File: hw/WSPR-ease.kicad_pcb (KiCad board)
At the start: 4 copper layers, 99 x 64 mm, 134 parts, among them J101 SMA, J102 SMA, J103 pwr+data, Q101 MMBF170, Q301 MMBF170, Q302 MMBF170, Q303 MMBF170, Q304 MMBF170, Q305 MMBF170, Q306 MMBF170, Q307 MMBF170, Q308 MMBF170, Q309 MMBF170, Q310 MMBF170, Q311 MMBF170, Q312 MMBF170, T301 BN-43-202_DualPri_CTSec, U101 GNSS module, U102 ESP32-S3-WROOM-1-N8R8, U103 SRV05-4, U104 TPS22918DBVR, U105 TPS74612PQWDRBRQ1, U106 LMR51430YDDCR, U201 AS183-92LF, U202 AS183-92LF, U203 AS183-92LF, U204 AS183-92LF, U301 ICE40UP5K-SG48ITR, U302 CD74ACT541SM96, Y301 40MHz

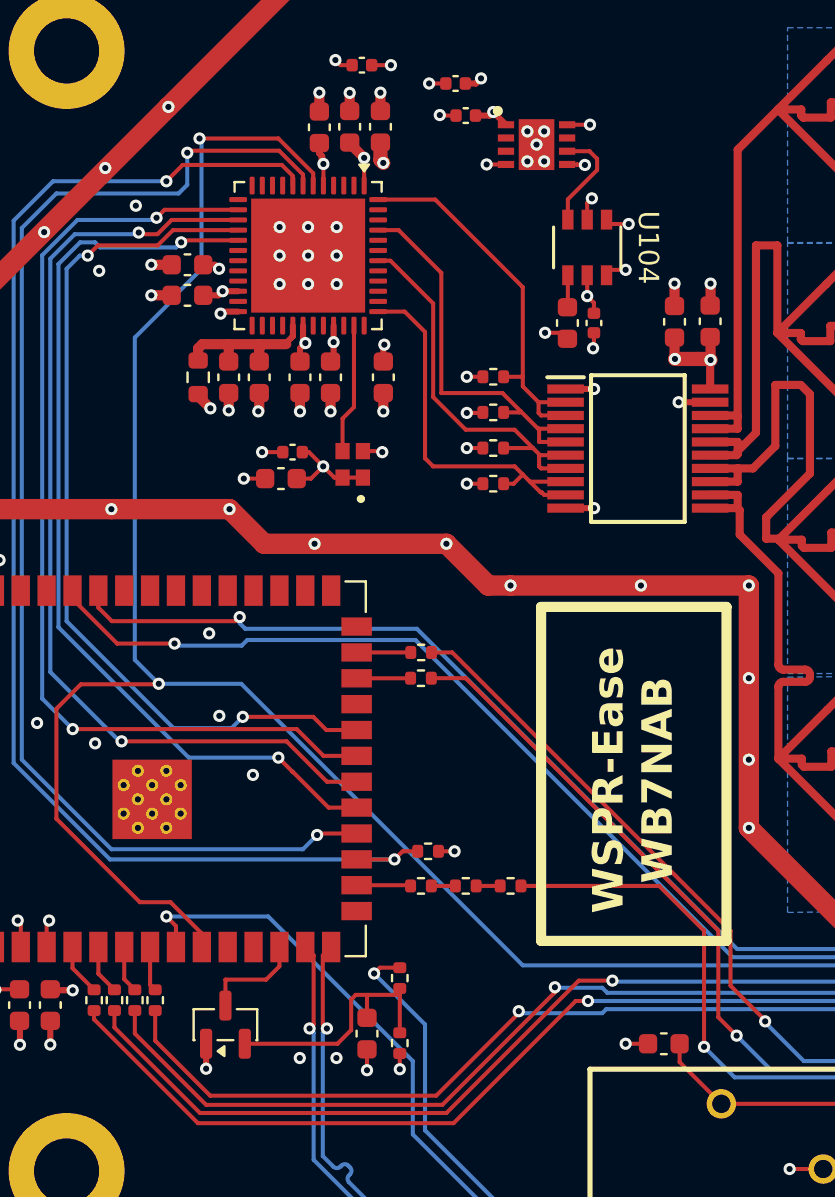
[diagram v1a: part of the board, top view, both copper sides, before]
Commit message: Still working on FPGA config loading. Problem is now CMOS lockup caused by FPGACORE vs FPGAIO rails. I moved FPGAIO enable to IO42 on ESP32 and pgFPGACORE to IO41.
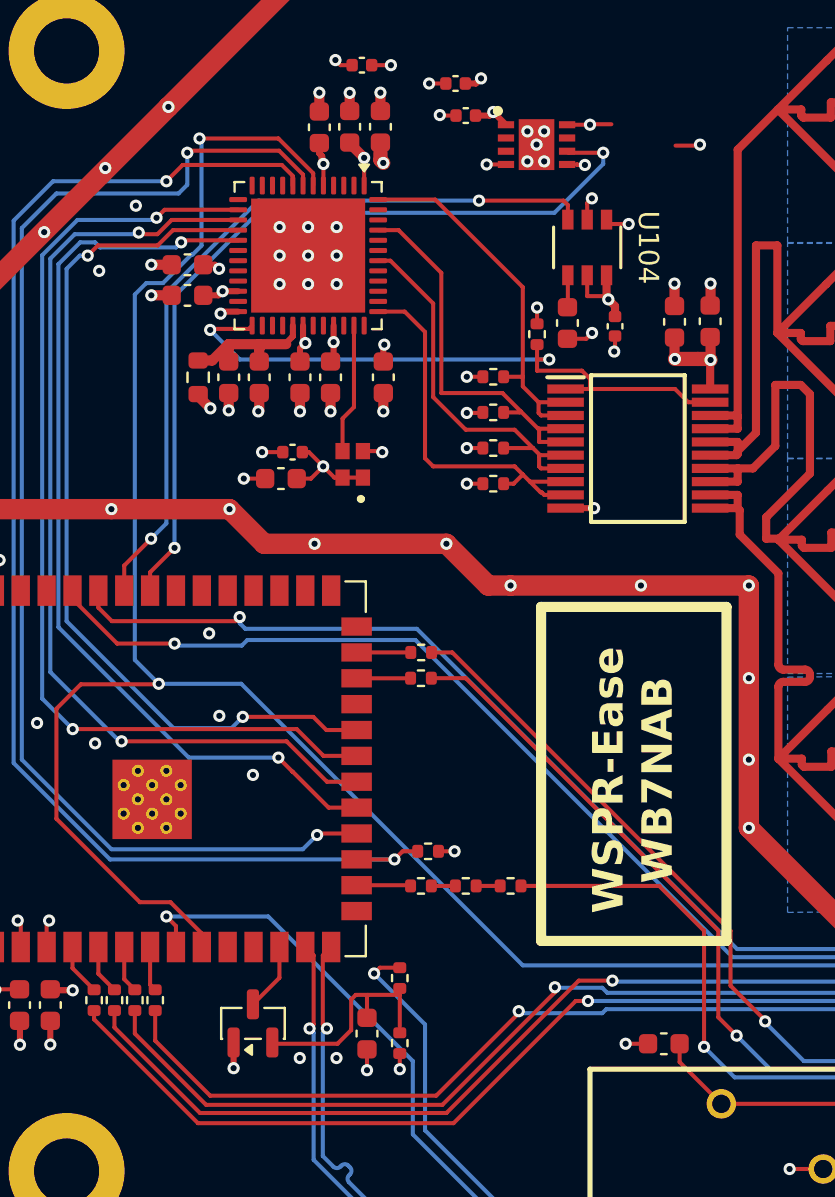
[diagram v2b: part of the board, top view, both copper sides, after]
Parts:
- added R319: 10k, Resistor_SMD:R_0402_1005Metric, F.Cu at (77.7, 87.3)
- moved Q101 1.35 mm to (63.8, 121.2)
- moved C109 1.05 mm to (81.5, 86.9)
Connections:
- U102 pad 34: unconnected-(U102-IO41-Pad34) -> /pgFPGACORE
- U102 pad 35: unconnected-(U102-IO42-Pad35) -> /enFPGAIO
- U104 pad 3: Net-(U104-ON) -> /enFPGAIO
- U105 pad 6: Net-(U104-ON) -> /pgFPGACORE
- U301 pad 25: unconnected-(U301A-IOT_36b-Pad25) -> /Transmitter/driverNEN
- U302 pad 1: GND -> /Transmitter/driverNEN
- U302 pad 19: GND -> /Transmitter/driverNEN
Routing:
- net /pgFPGACORE: track 0.00 -> 41.1 mm, vias 0 -> 2
- net /enFPGAIO: track 0.00 -> 37.9 mm, vias 0 -> 2
- net /Transmitter/driverNEN: track 0.00 -> 31.9 mm, vias 0 -> 2
- net Net-(U104-ON): track 5.44 -> 0.00 mm
- net +3.3V: track 23.1 -> 25.0 mm, vias 16 -> 17
- net Net-(Q101-D): track 5.14 -> 3.35 mm
- net GND: track 336.9 -> 335.4 mm, vias 162 -> 161
- net +VFPGAIO: track 22.5 -> 23.9 mm, vias 12 -> 11
- net Net-(Q101-S): track 12.2 -> 10.8 mm
- net /gnssPPS: track 131.2 -> 131.7 mm

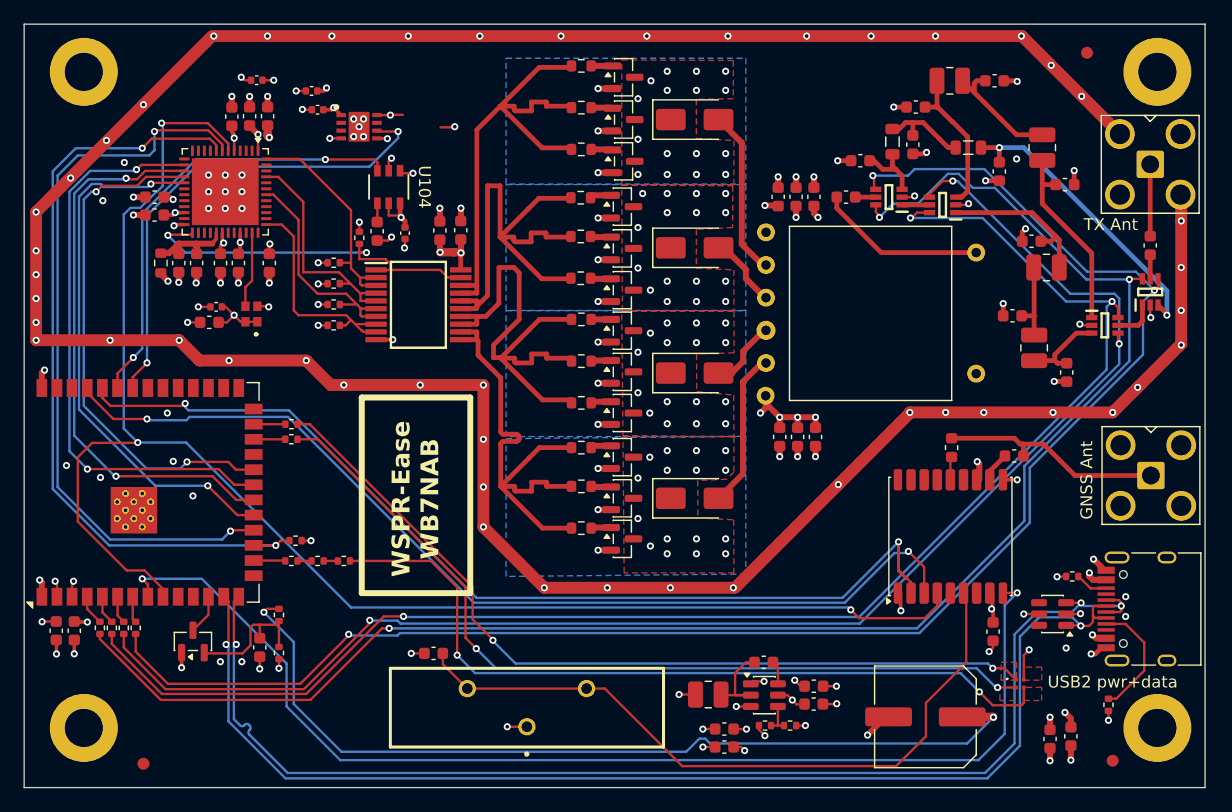
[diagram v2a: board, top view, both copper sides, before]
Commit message: Rename-o-rama to make coding style match my explicit guidelines (GEMINI ignores these for some reason). I have cleaned a few things up in the process. Code is somewhat broken right now as I prep for FPGA loading.
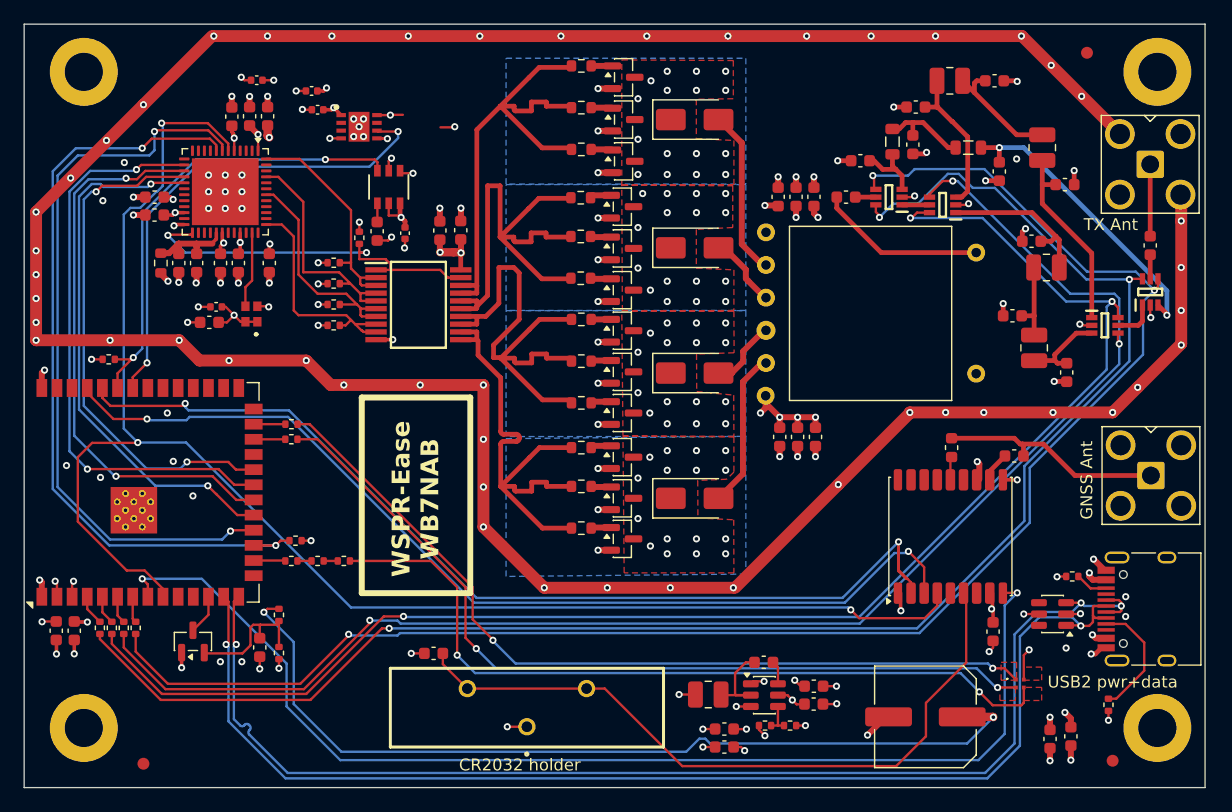
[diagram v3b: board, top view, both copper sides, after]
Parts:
- added R116: 10k, Resistor_SMD:R_0402_1005Metric, F.Cu at (56.7, 97.5)
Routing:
- net /enFPGAIO: track 37.9 -> 39.5 mm
- net GND: track 335.4 -> 336.4 mm, vias 161 -> 162
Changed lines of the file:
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@@
 			)
 		)
+		(property "label" "CR2032 holder"
+			(at 0.6 -4.8 0)
+			(unlocked yes)
+			(layer "F.SilkS")
+			(effects
+				(font
+					(size 1 1)
+					(thickness 0.15)
+				)
+			)
+		)
 		(sheetname "/")
 		(sheetfile "WSPR-ease.kicad_sch")
@@
 			(unlocked yes)
 			(layer "F.SilkS")
+			(hide yes)
 			(effects
 				(font
@@
 		(embedded_fonts no)
 	)
+	(footprint "Resistor_SMD:R_0402_1005Metric"
+		(layer "F.Cu")
+		(at 56.69 97.5)
+		(descr "Resistor SMD 0402 (1005 Metric), square (rectangular) end terminal, IPC-7351 nominal, (Body size source: IPC-SM-782 page 72, https://www.pcb-3d.com/wordpress/wp-content/uploads/ipc-sm-782a_amendment_1_and_2.pdf), generated with kicad-footprint-generator")
+		(tags "resistor")
+		(property "Reference" "R116"
+			(at 0 -1.17 0)
+			(layer "F.SilkS")
+			(hide yes)
+			(effects
+				(font
+					(size 1 1)
+					(thickness 0.15)
+				)
+			)
+		)
+		(property "Value" "10k"
+			(at 0 1.17 0)
+			(layer "F.Fab")
+			(effects
+				(font
+					(size 1 1)
+					(thickness 0.15)
+				)
+			)
+		)
+		(property "Datasheet" "~"
+			(at 0 0 0)
+			(layer "F.Fab")
+			(hide yes)
+			(effects
+				(font
+					(size 1.27 1.27)
+					(thickness 0.15)
+				)
+			)
+		)
+		(property "Description" "Resistor, small US symbol"
+			(at 0 0 0)
+			(layer "F.Fab")
+			(hide yes)
+			(effects
+				(font
+					(size 1.27 1.27)
+					(thickness 0.15)
+				)
+			)
+		)
+		(property ki_fp_filters "R_*")
+		(sheetname "/")
+		(sheetfile "WSPR-ease.kicad_sch")
+		(attr smd)
+		(fp_line
+			(start -0.153641 -0.38)
+			(end 0.153641 -0.38)
+			(stroke
+				(width 0.12)
+				(type solid)
+			)
+			(layer "F.SilkS")
+		)
+		(fp_line
+			(start -0.153641 0.38)
+			(end 0.153641 0.38)
+			(stroke
+				(width 0.12)
+				(type solid)
+			)
+			(layer "F.SilkS")
+		)
+		(fp_rect
+			(start -0.93 -0.47)
+			(end 0.93 0.47)
+			(stroke
+				(width 0.05)
+				(type solid)
+			)
+			(fill no)
+			(layer "F.CrtYd")
+		)
+		(fp_rect
+			(start -0.525 -0.27)
+			(end 0.525 0.27)
+			(stroke
+				(width 0.1)
+				(type solid)
+			)
+			(fill no)
+			(layer "F.Fab")
+		)
+		(fp_text user "${REFERENCE}"
+			(at 0 0 0)
+			(layer "F.Fab")
+			(effects
+				(font
+					(size 0.26 0.26)
+					(thickness 0.04)
+				)
+			)
+		)
+		(pad "1" smd roundrect
+			(at -0.51 0)
+			(size 0.54 0.64)
+			(layers "F.Cu" "F.Mask" "F.Paste")
+			(roundrect_rratio 0.25)
+			(net 1 "GND")
+			(pintype "passive")
+		)
+		(pad "2" smd roundrect
+			(at 0.51 0)
+			(size 0.54 0.64)
+			(layers "F.Cu" "F.Mask" "F.Paste")
+			(roundrect_rratio 0.25)
+			(net 147 "/enFPGAIO")
+			(pintype "passive")
+		)
+		(embedded_fonts no)
+		(model "${KICAD9_3DMODEL_DIR}/Resistor_SMD.3dshapes/R_0402_1005Metric.step"
+			(offset
+				(xyz 0 0 0)
+			)
+			(scale
+				(xyz 1 1 1)
+			)
+			(rotate
+				(xyz 0 0 0)
+			)
+		)
+	)
 	(footprint "Package_TO_SOT_SMD:SOT-23-6"
 		(layer "F.Cu")
@@
 	)
 	(segment
+		(start 56.18 97.5)
+		(end 55.25 97.5)
+		(width 0.2)
+		(layer "F.Cu")
+		(net 1)
+	)
+	(segment
 		(start 68.5 76.35)
 		(end 68.5 75.46)
@@
 	)
 	(via
+		(at 55.25 97.5)
+		(size 0.6)
+		(drill 0.3)
+		(layers "F.Cu" "B.Cu")
+		(net 1)
+	)
+	(via
 		(at 73.65 112.7)
 		(size 0.6)
@@
 		(width 0.2)
 		(layer "F.Cu")
+		(net 147)
+	)
+	(segment
+		(start 58.6 97.5)
+		(end 58.75 97.35)
+		(width 0.2)
+		(layer "F.Cu")
+		(net 147)
+	)
+	(segment
+		(start 57.2 97.5)
+		(end 58.6 97.5)
+		(width 0.2)
+		(layer "F.Cu")

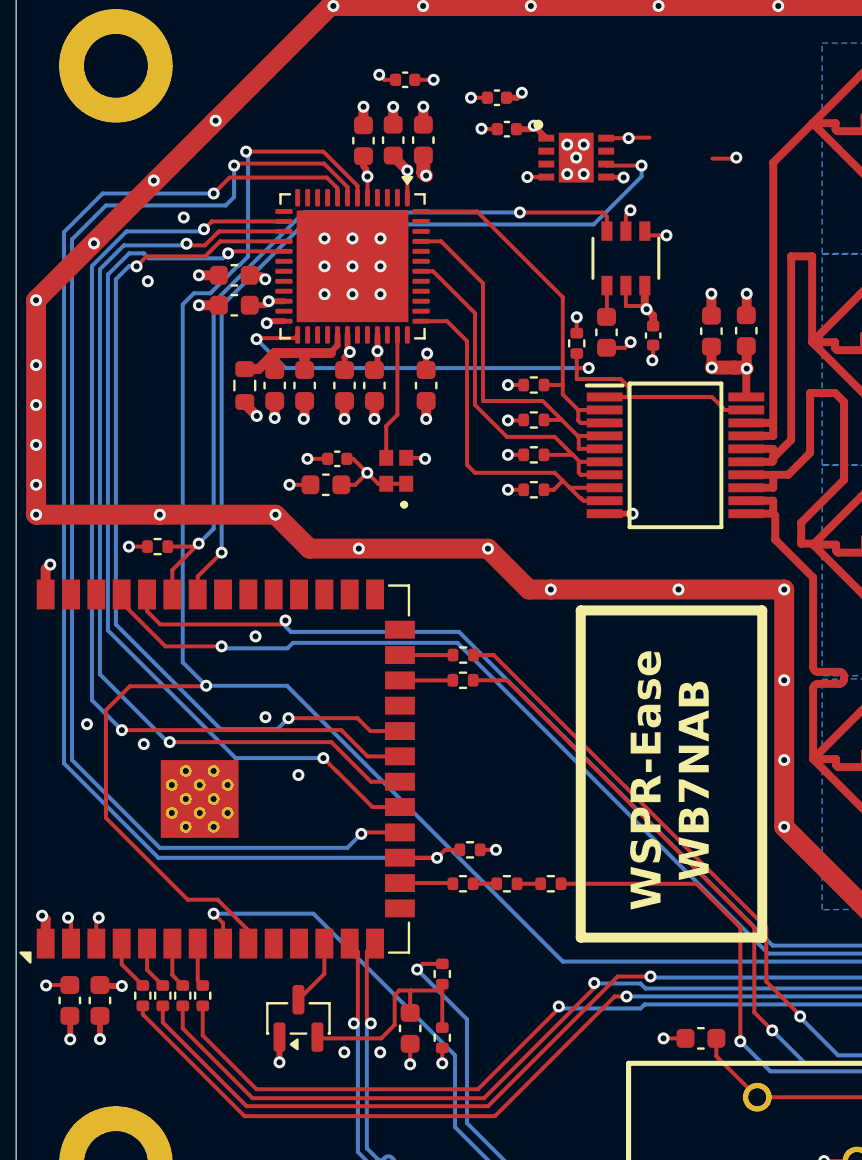
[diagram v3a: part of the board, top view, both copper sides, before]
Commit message: Add 10k pullup to +3.3V for PG on FPGA CORE rail so we can read it from ESP32.
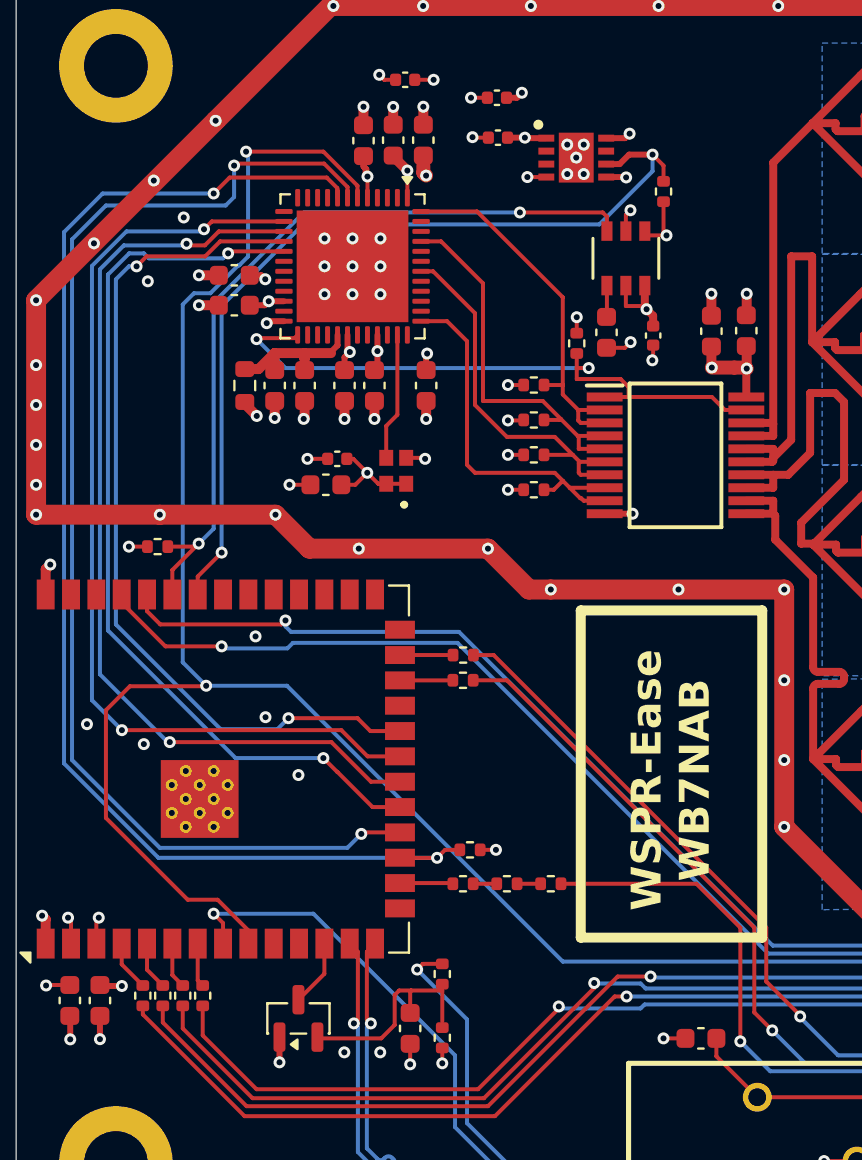
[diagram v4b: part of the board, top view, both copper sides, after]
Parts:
- added R117: 10k, Resistor_SMD:R_0402_1005Metric, F.Cu at (82.0, 79.7)
- moved C108 0.62 mm to (73.8, 77.0)
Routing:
- net /pgFPGACORE: track 41.1 -> 44.3 mm
- net GND: track 336.4 -> 335.1 mm, vias 162 -> 161
- net +3.3V: track 25.0 -> 26.2 mm
